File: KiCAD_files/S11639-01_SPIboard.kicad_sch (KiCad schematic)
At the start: 60 parts, among them IC1 74LVC1T45GW,125, IC2 74LVC1T45GW,125, IC3 74LVC1T45GW,125, IC4 MCP33131D-10-I_MS, IC5 74LVC1T45GW,125, J1 Conn_01x03_Male, J2 Conn_02x10_Odd_Even, J3 705430001, J4 Conn_01x03_Male, U1 ADA4807-2ARMZ-R7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

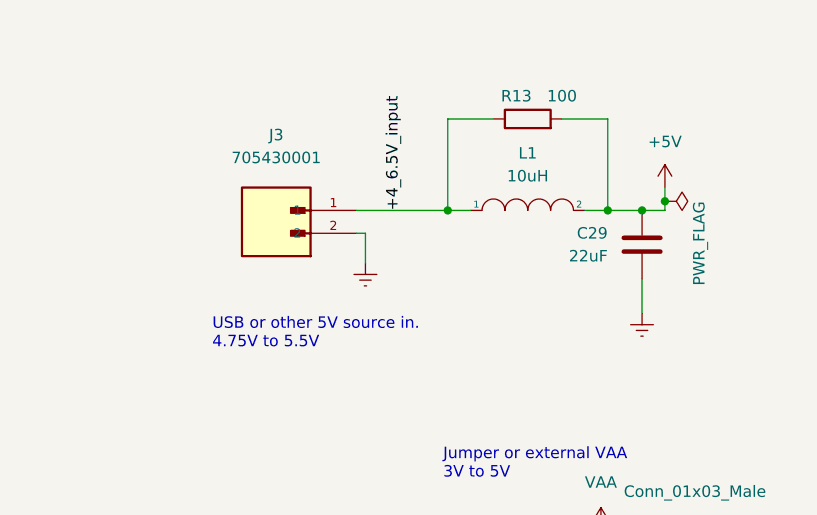
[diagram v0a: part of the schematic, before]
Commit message: upgrade input power filter
Adds input side cap to the inductive input filter.
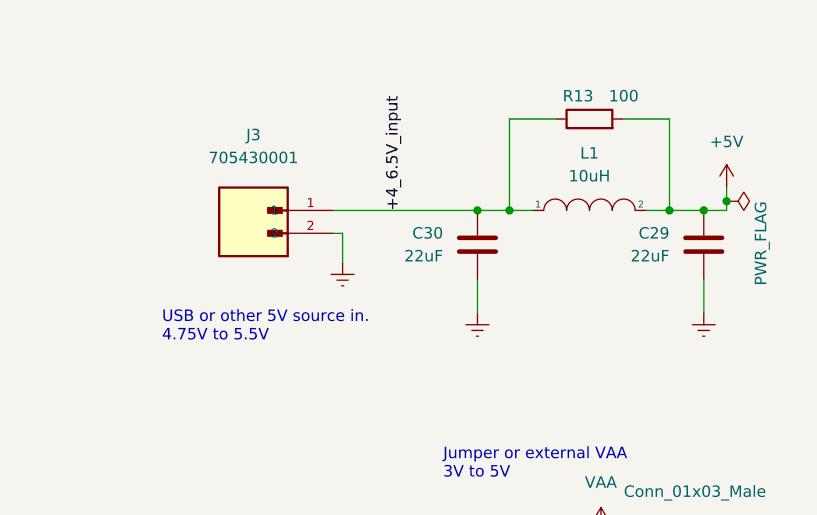
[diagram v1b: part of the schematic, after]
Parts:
- added C30: 22uF, Capacitor_SMD:C_0805_2012Metric, symbol Device:C
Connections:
- net +4_6.5V_input: now also C30.1
- net Earth: now also C30.2
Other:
- moved on the sheet: C29, J3, L1, R13
